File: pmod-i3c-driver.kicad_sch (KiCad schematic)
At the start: 77 parts, among them J1 PinSocket_2x12_P2.54mm_Drill1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, J2 PinSocket_2x6_P2.54mm_Drill1.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, J3 JST_SH_1x4_SM04B-SRSS-TB-LF-SN, J4 USB-C_CUI_UJC-HP-3-SMT-TR, J5 PinHeader_1x3_P2.54mm_Drill1.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, J6 PinHeader_1x3_P2.54mm_Drill1.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, J7 PinHeader_2x10_P1.27mm_SMD, Q1 DMC31D5UDJ, Q2 DMC31D5UDJ, Q3 DMC2400UV-7, Q4 DMC2400UV-7, Q5 DMG1012T-7, U1 TPS7A0518P_SOT23-5, U2 SN74LVC1G240_SC70, U3 SN74LVC1G240_SC70, U4 TLV70033_SC70

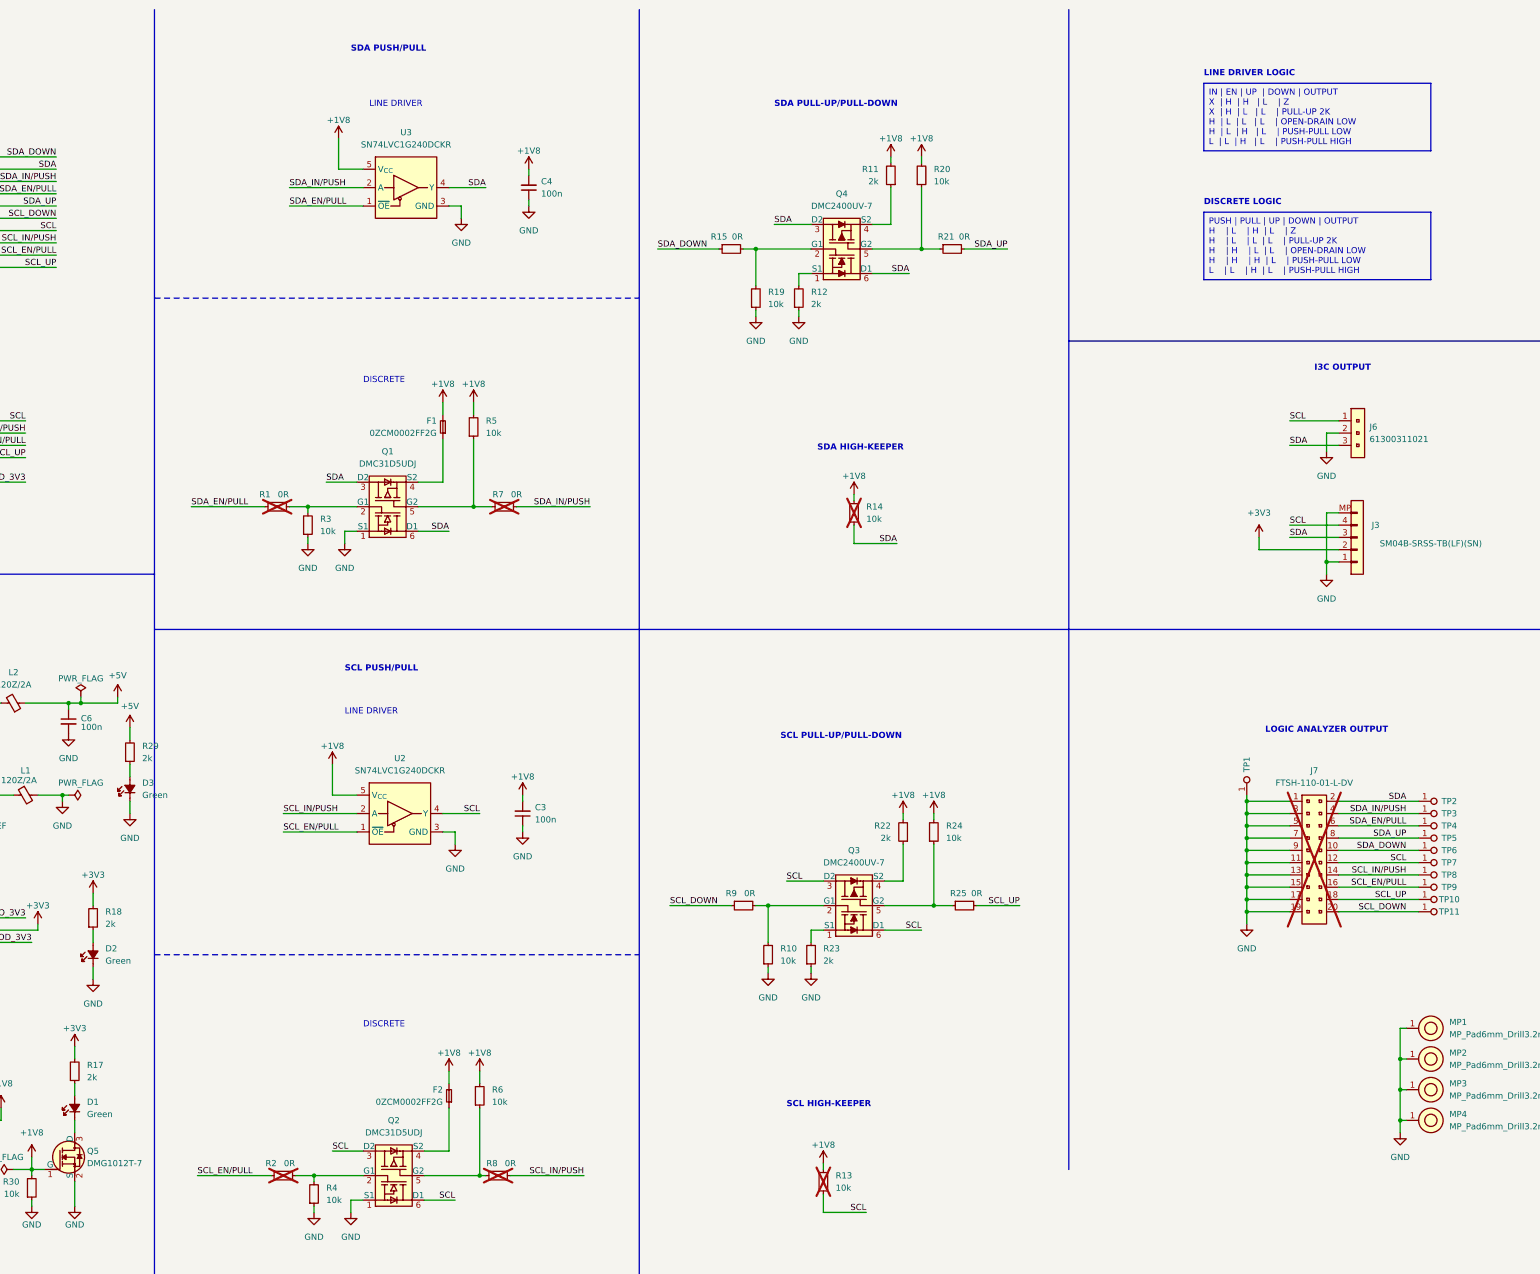
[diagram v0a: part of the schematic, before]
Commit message: [#80692] Update symbols, fix ERC
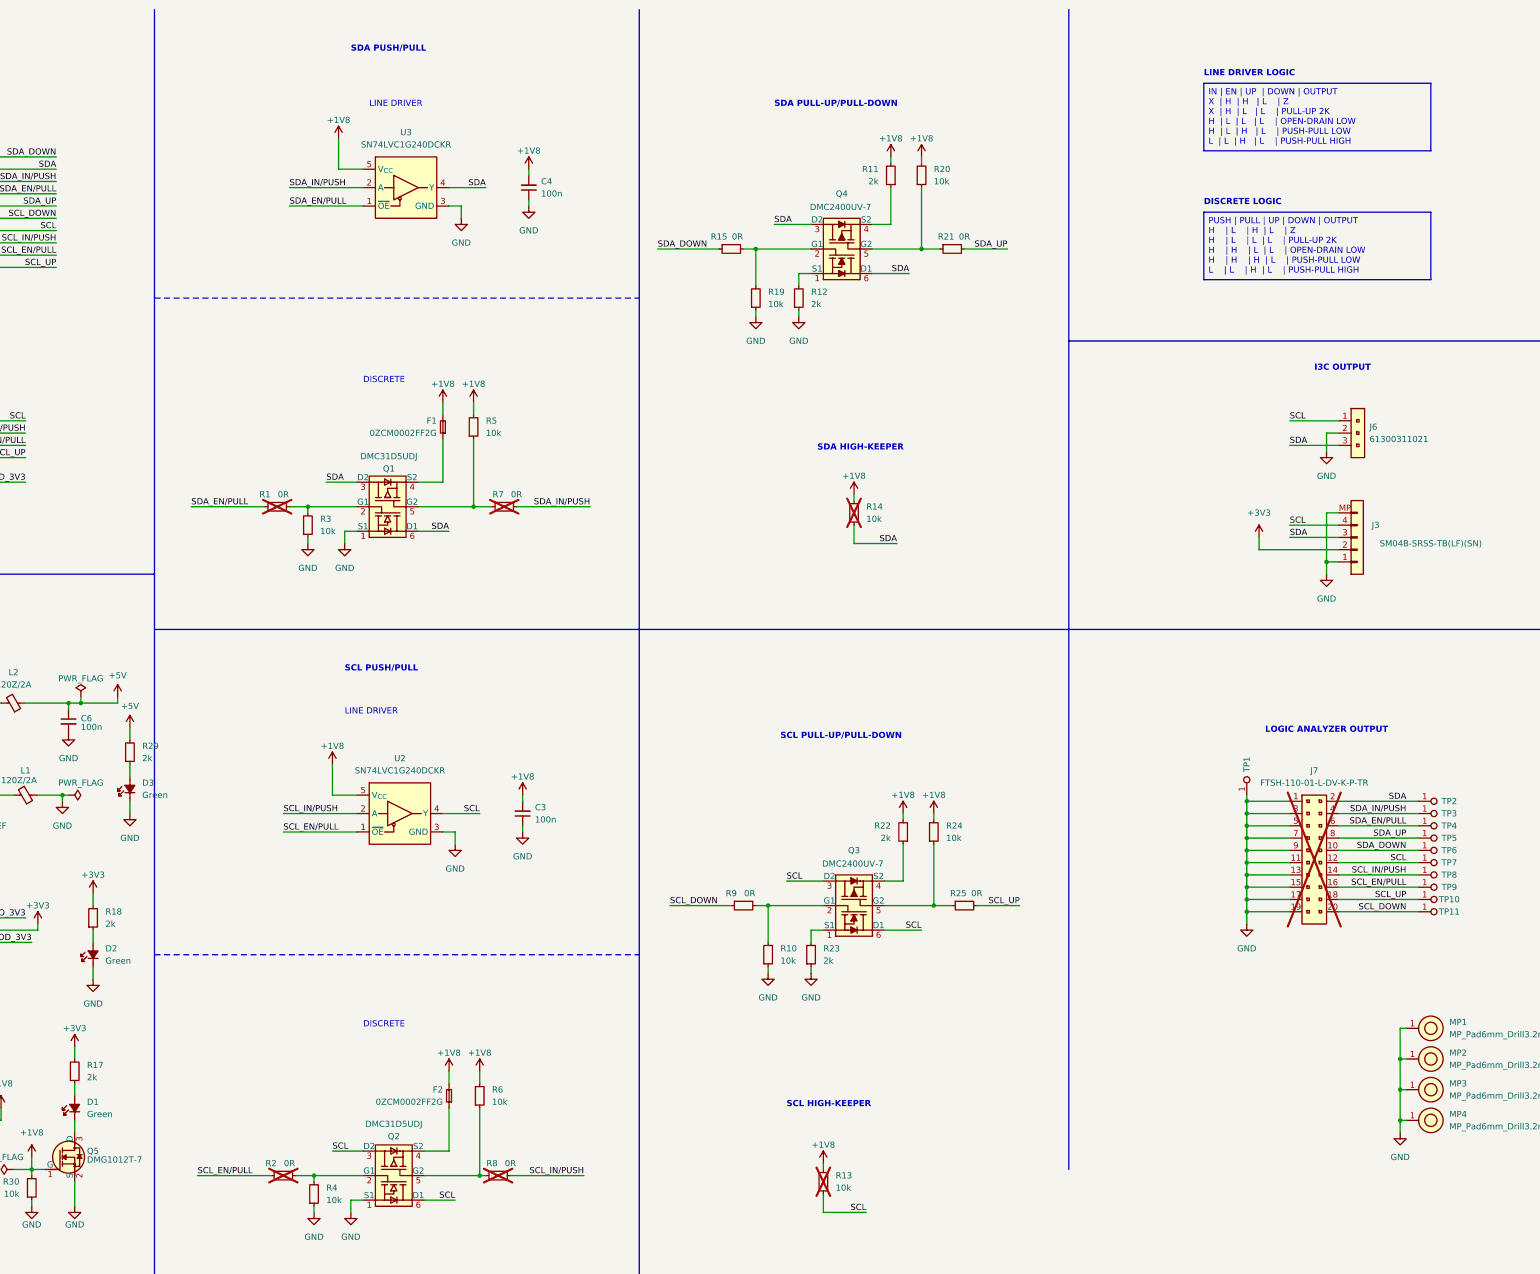
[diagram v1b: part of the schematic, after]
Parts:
- removed J7: PinHeader_2x10_P1.27mm_SMD, antmicro-footprints:PinHeader_2x10_P1.27mm_SMD, symbol antmicroGenericPinHeaders:PinHeader_2x10_P1.27mm_SMD
- added J7: PinHeader_2x10_P1.27mm_SMD_Latch, antmicro-footprints:PinHeader_2x10_P1.27mm_SMD_Latch, symbol antmicroGenericPinHeaders:PinHeader_2x10_P1.27mm_SMD_Latch
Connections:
- net GND: now also J7.1, J7.11, J7.13, J7.15, J7.17, J7.19, J7.3, J7.5, J7.7, J7.9
- net SCL: now also J7.12
- net SCL_DOWN: now also J7.20
- net SCL_EN/PULL: now also J7.16
- net SCL_IN/PUSH: now also J7.14
- net SCL_UP: now also J7.18
- net SDA: now also J7.2
- net SDA_DOWN: now also J7.10
- net SDA_EN/PULL: now also J7.6
- net SDA_IN/PUSH: now also J7.4
- net SDA_UP: now also J7.8

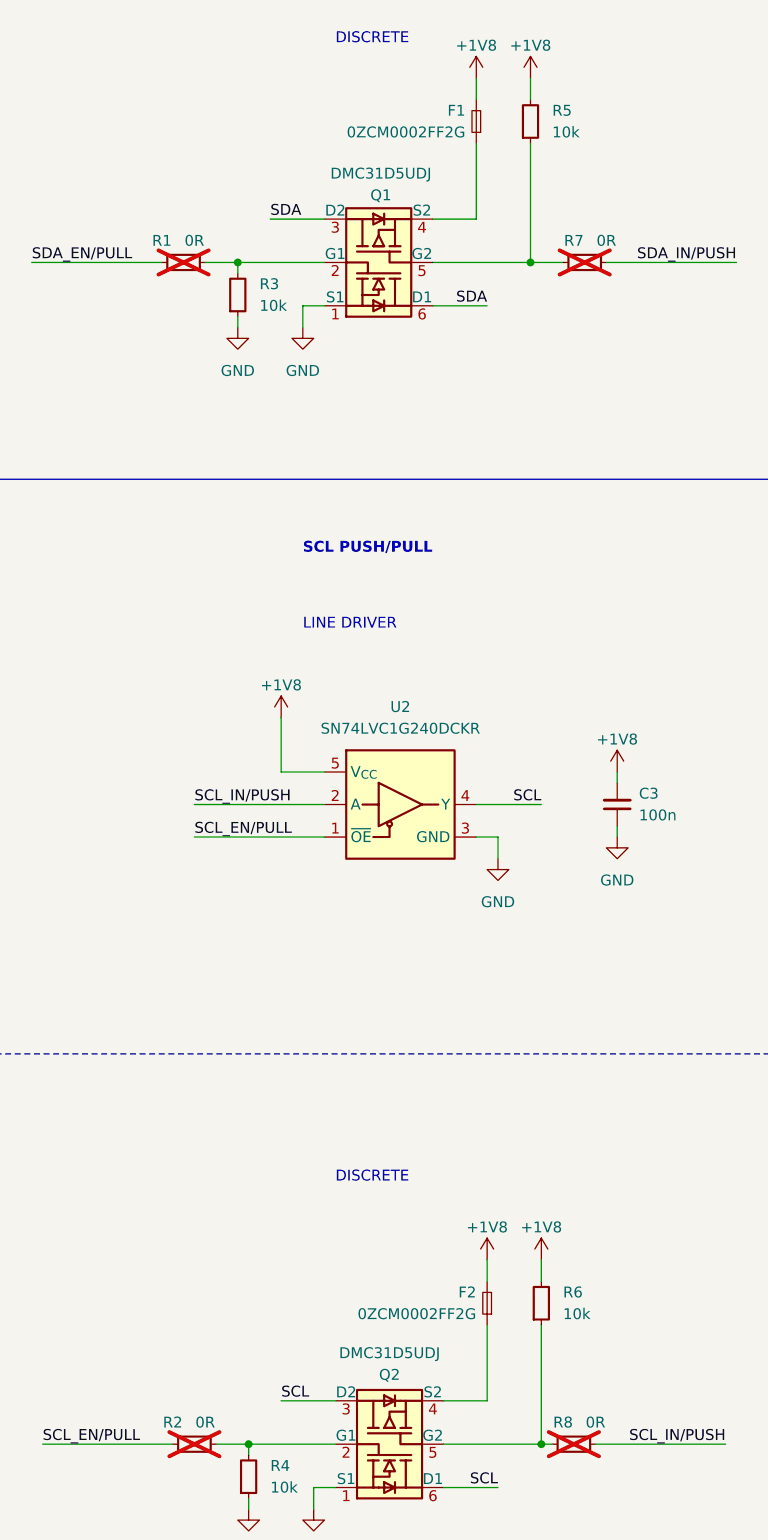
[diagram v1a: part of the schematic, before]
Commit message: [#80692] Update footprints, clean ERC, bump rev to 1.0.1
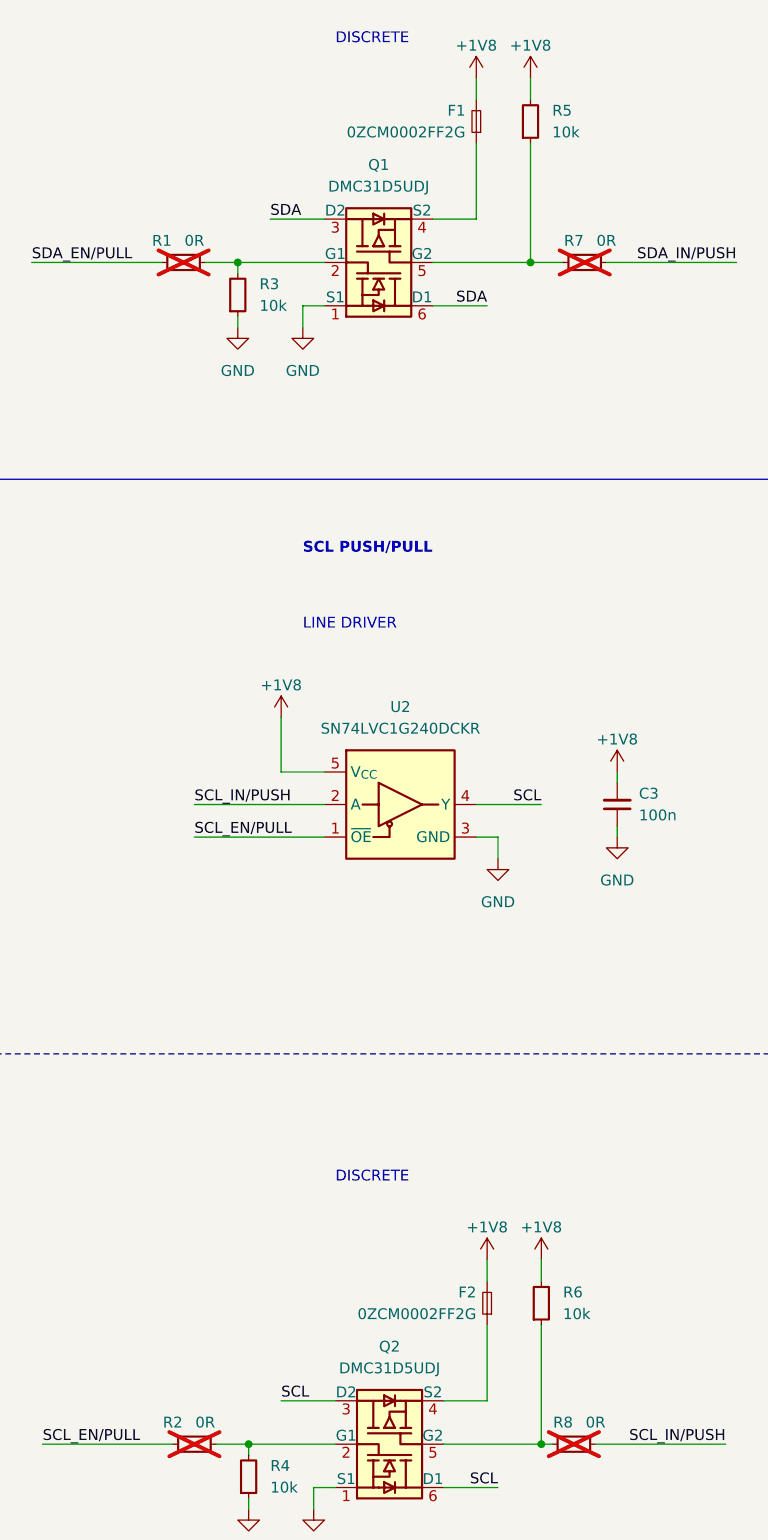
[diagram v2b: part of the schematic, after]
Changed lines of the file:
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@@
 	(title_block
 		(title "PMOD I3C Driver")
-		(date "2024-11-05")
-		(rev "1.0.0")
+		(date "2025-07-22")
+		(rev "1.0.1")
 		(company "Antmicro Ltd.")
 		(comment 1 "www.antmicro.com")
@@
 			)
 		)
-		(property "Description" ""
+		(property "Description" "Pin Socket 2.54mm, 2 Rows, 24 Contacts, Through Hole Mount"
 			(at 69.85 53.34 0)
 			(effects
@@
 		(on_board yes)
 		(dnp no)
-		(fields_autoplaced yes)
 		(property "Reference" "F1"
 			(at 168.91 97.79 90)
@@
 	)
 	(symbol
-		(lib_name "DMC31D5UDJ_1")
 		(lib_id "antmicroTransistorsFETsMOSFETsArrays:DMC31D5UDJ")
 		(at 153.67 248.92 0)
@@
 		(on_board yes)
 		(dnp no)
+		(fields_autoplaced yes)
 		(property "Reference" "Q2"
-			(at 160.02 245.872 0)
+			(at 160.02 242.57 0)
 			(effects
 				(font
@@
 			)
 		)
-		(property "Description" ""
-			(at 187.96 266.7 0)
+		(property "Description" "Dual MOSFET, N and P channel, 30V, 0.2A"
+			(at 174.752 261.62 0)
 			(effects
 				(font
@@
 		)
 		(property "MPN" "DMC31D5UDJ"
-			(at 160.02 243.332 0)
+			(at 160.02 245.11 0)
 			(effects
 				(font
@@
 		(exclude_from_sim no)
 		(in_bom no)
-		(on_board no)
+		(on_board yes)
 		(dnp yes)
 		(fields_autoplaced yes)
@@
 		(on_board yes)
 		(dnp no)
+		(fields_autoplaced yes)
 		(property "Reference" "Q1"
-			(at 159.004 107.696 0)
+			(at 158.75 104.14 0)
 			(effects
 				(font
@@
 			)
 		)
-		(property "Description" ""
-			(at 186.69 128.27 0)
+		(property "Description" "Dual MOSFET, N and P channel, 30V, 0.2A"
+			(at 173.482 123.19 0)
 			(effects
 				(font
@@
 		)
 		(property "MPN" "DMC31D5UDJ"
-			(at 159.004 105.156 0)
+			(at 158.75 106.68 0)
 			(effects
 				(font
